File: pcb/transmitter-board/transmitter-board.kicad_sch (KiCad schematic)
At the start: 26 parts, among them J1 USB-C_USB-310F-B-SU, Q3 AO3400A, Q4 AO3400A, SW1 SW_DPDT_x2, U1 NE555D, U3 TP4056-42-ESOP8, U4 DW01A

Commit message: Refactor transmitter-board schematic
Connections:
- net OUT+: now also BT1.1 (+), C7.1, R10.1
- net VBUS: no longer BT1.1 (+), C7.1, R10.1
- net 555OUT: no longer names the net of R8.1, U1.3 (Q)
- net B-: no longer names the net of BT1.2 (-), C6.2, Q4.2 (S), U4.6 (GND)
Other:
- moved on the sheet: BT1, C4, C6, C7, D1, D2, D3, J1, Q3, Q4, R10, R3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

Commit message: Final refactor transmitter-board schematic
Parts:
- U3: value TP4056-42-ESOP8 -> TP4056
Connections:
- net OUT+: no longer names the net of BT1.1 (+), C7.1, R10.1, SW1.2 (B), U3.5 (BAT)
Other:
- moved on the sheet: BT1, C1, C2, C4, C6, C7, D1, D2, D3, J1, Q3, Q4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

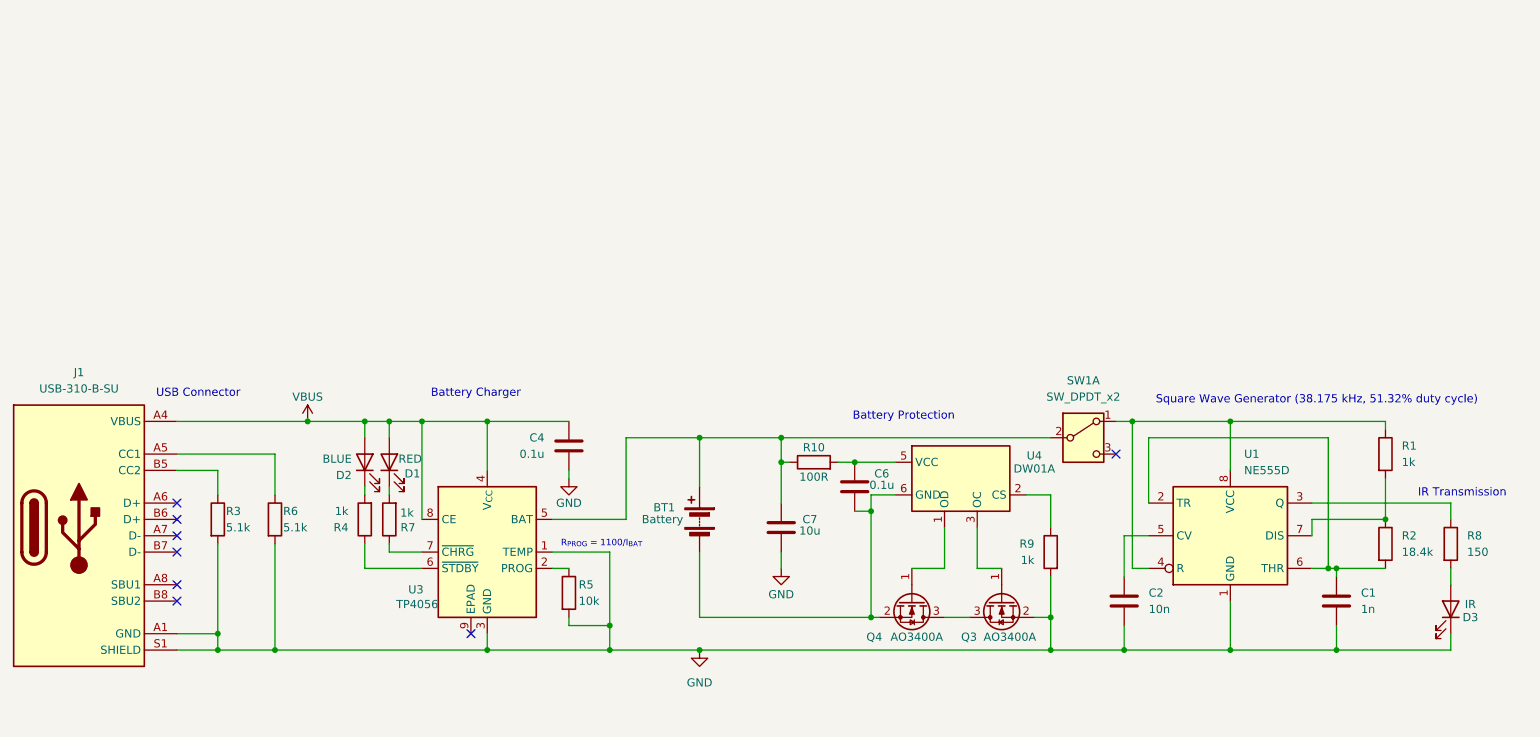
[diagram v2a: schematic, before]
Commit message: Clear ERC and DRC
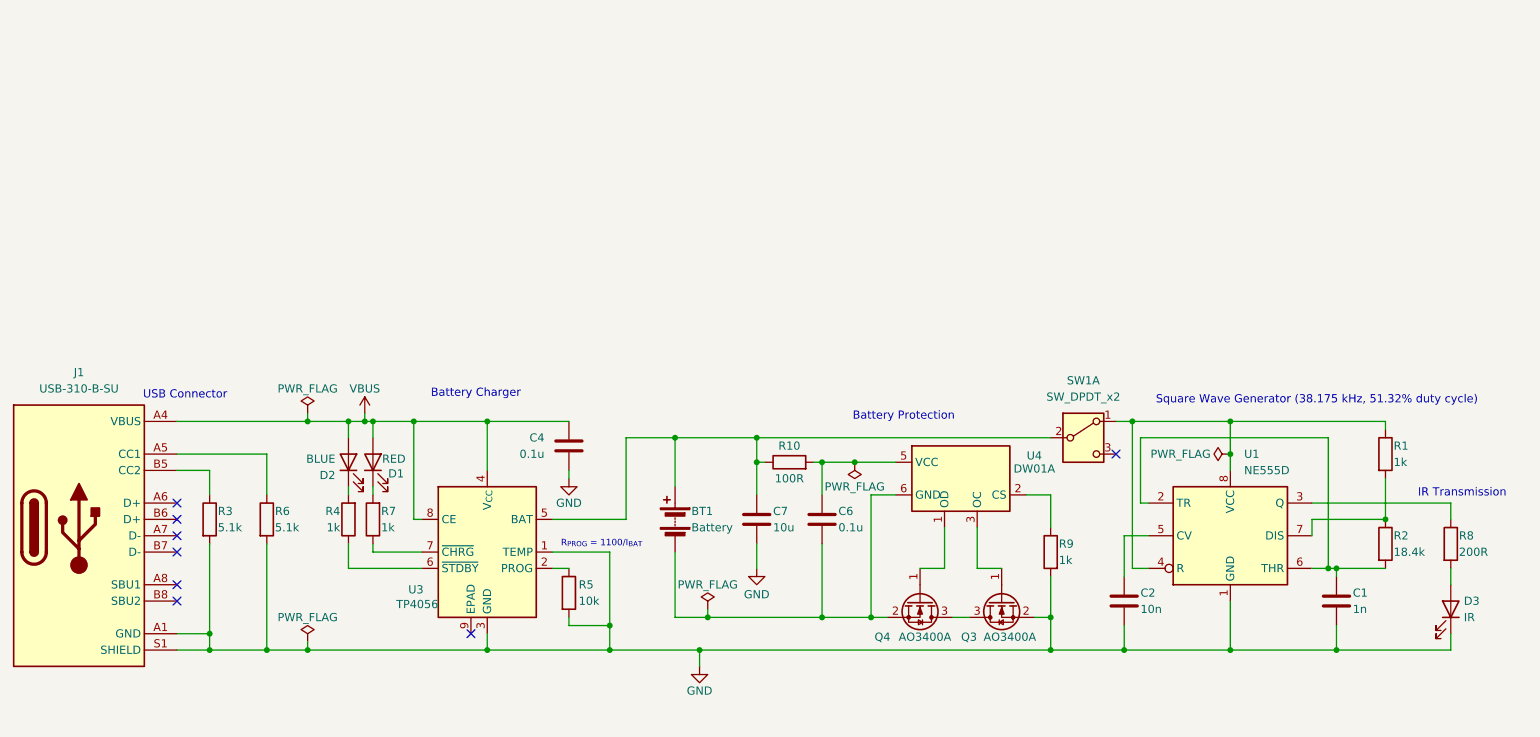
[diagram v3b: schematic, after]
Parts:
- R8: value 150 -> 200R
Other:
- moved on the sheet: BT1, C6, C7, D1, D2, Q4, R10, R3, R4, R6, R7
